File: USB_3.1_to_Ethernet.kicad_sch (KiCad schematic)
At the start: 5 parts, among them J1 RJ45_JK0654219, U1 LAN7801_9JX, U2 93LC56B_SN, U3 KSZ9031RNXCC, U4 TLV76733QWDRBxQ1

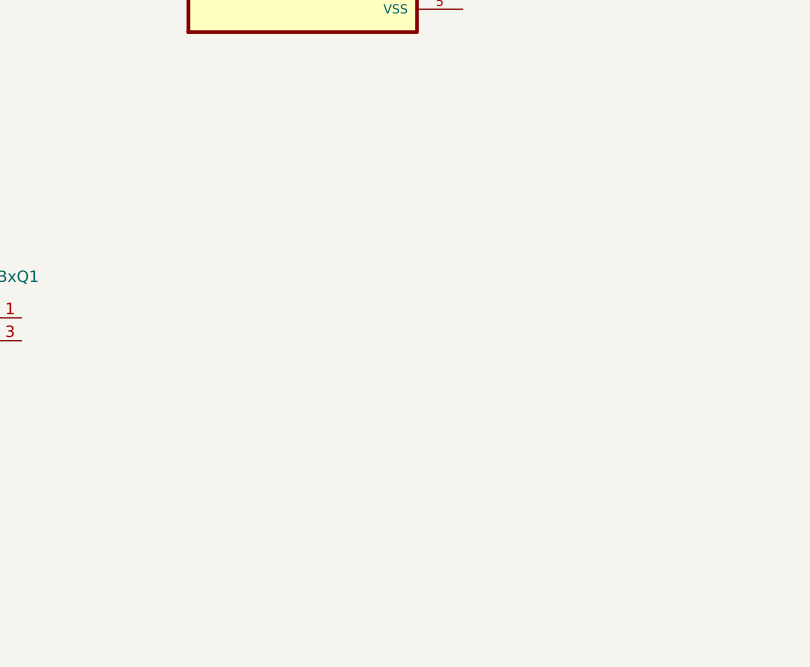
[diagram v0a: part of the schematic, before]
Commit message: usb connector added
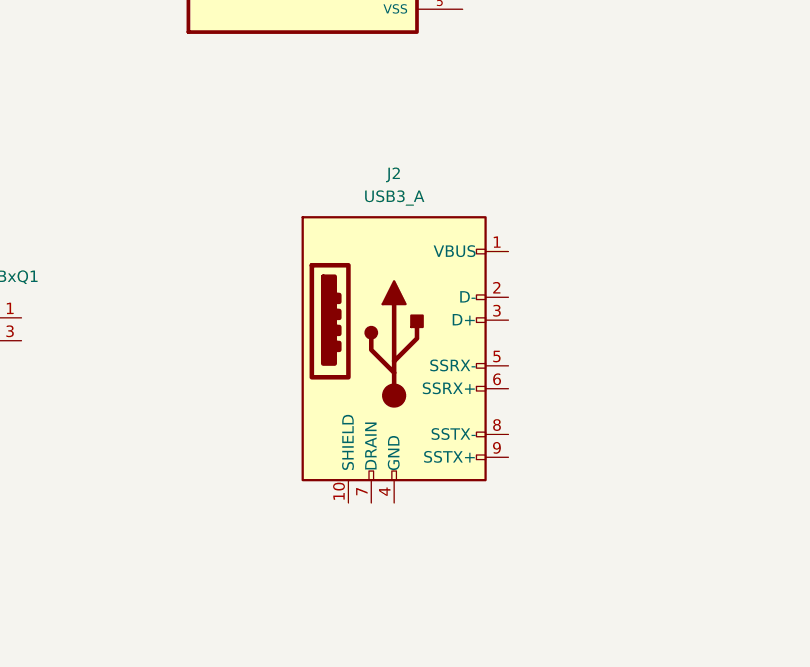
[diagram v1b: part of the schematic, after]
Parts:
- added J2: USB3_A, Connector_USB:USB3_A_Plug_Wuerth_692112030100_Horizontal, symbol Connector:USB3_A
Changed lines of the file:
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@@
+	)
+	(symbol
+		(lib_id "Connector:USB3_A")
+		(at 159.258 119.126 0)
+		(unit 1)
+		(exclude_from_sim no)
+		(in_bom yes)
+		(on_board yes)
+		(dnp no)
+		(fields_autoplaced yes)
+		(property "Reference" "J2"
+			(at 159.258 100.33 0)
+			(effects
+				(font
+					(size 1.27 1.27)
+				)
+			)
+		)
+		(property "Value" "USB3_A"
+			(at 159.258 102.87 0)
+			(effects
+				(font
+					(size 1.27 1.27)
+				)
+			)
+		)
+		(property "Footprint" "Connector_USB:USB3_A_Plug_Wuerth_692112030100_Horizontal"
+			(at 163.068 116.586 0)
+			(effects
+				(font
+					(size 1.27 1.27)
+				)
+				(hide yes)
+			)
+		)
+		(property "Datasheet" "~"
+			(at 163.068 116.586 0)
+			(effects
+				(font
+					(size 1.27 1.27)
+				)
+				(hide yes)
+			)
+		)
+		(property "Description" "USB 3.0 A connector"
+			(at 159.258 119.126 0)
+			(effects
+				(font
+					(size 1.27 1.27)
+				)
+				(hide yes)
+			)
+		)
+		(pin "4"
+		)
+		(pin "7"
+		)
+		(pin "3"
+		)
+		(pin "5"
+		)
+		(pin "1"
+		)
+		(pin "2"
+		)
+		(pin "8"
+		)
+		(pin "9"
+		)
+		(pin "6"
+		)
+		(pin "10"
+		)
+		(instances
+			(project ""
+				(path "/b00c1253-ab18-4b3e-8546-134ebc6e3f42"
+					(reference "J2")
+					(unit 1)
+				)
+			)
+		)
 	)
 	(symbol

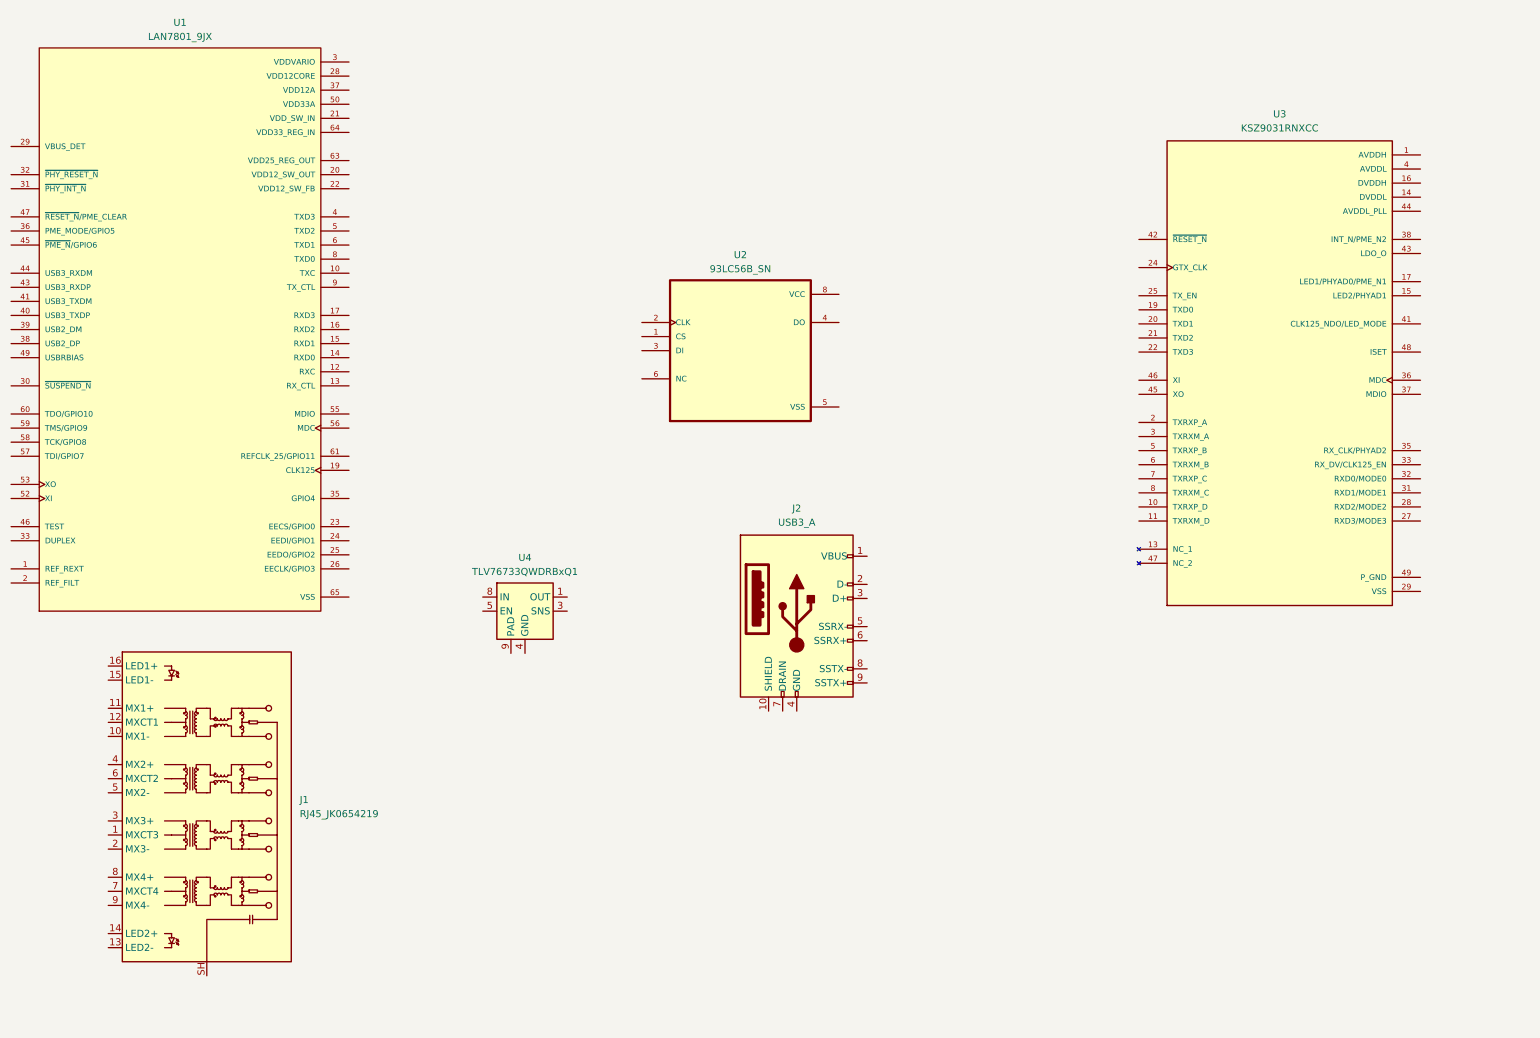
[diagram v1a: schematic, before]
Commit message: tvs-FB-ldo-symbol-footprint
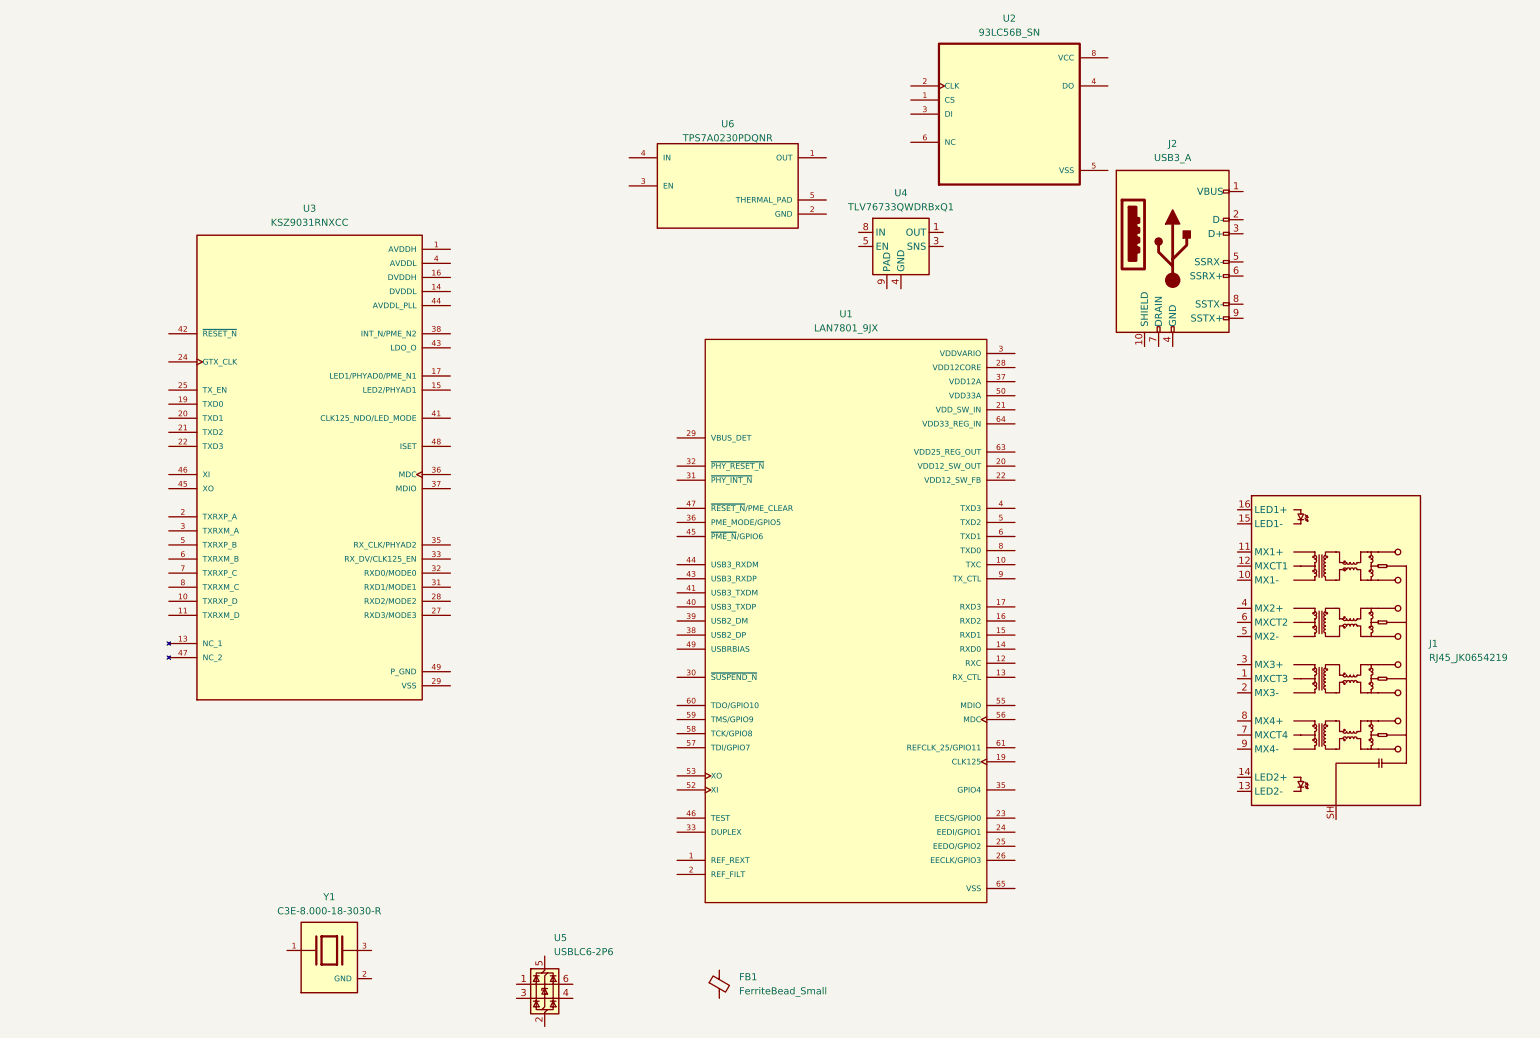
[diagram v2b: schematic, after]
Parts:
- added FB1: FerriteBead_Small, Inductor_SMD:L_0603_1608Metric_Pad1.05x0.95mm_HandSolder, symbol Device:FerriteBead_Small
- added U5: USBLC6-2P6, Package_TO_SOT_SMD:SOT-666, symbol Power_Protection:USBLC6-2P6
- added U6: TPS7A0230PDQNR, TPS7A0230PDQNR:IC_TPS7A0230PDQNR, symbol TPS7A0230PDQNR:TPS7A0230PDQNR
- added Y1: C3E-8.000-18-3030-R, C3E-8.000-18-3030-R:XTAL_C3E-8.000-18-3030-R, symbol C3E-8.000-18-3030-R:C3E-8.000-18-3030-R
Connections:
- new net GND: Y1.2 (GND), Y1.4 (GND)
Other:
- moved on the sheet: J1, J2, U1, U2, U3, U4

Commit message: power section added and power connections done
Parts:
- removed FB1: FerriteBead_Small, Inductor_SMD:L_0603_1608Metric_Pad1.05x0.95mm_HandSolder, symbol Device:FerriteBead_Small
- removed J2: USB3_A, Connector_USB:USB3_A_Plug_Wuerth_692112030100_Horizontal, symbol Connector:USB3_A
- removed U4: TLV76733QWDRBxQ1, Package_SON:VSON-8-1EP_3x3mm_P0.65mm_EP1.65x2.4mm_ThermalVias, symbol Regulator_Linear:TLV76733QWDRBxQ1
- removed U5: USBLC6-2P6, Package_TO_SOT_SMD:SOT-666, symbol Power_Protection:USBLC6-2P6
- removed U6: TPS7A0230PDQNR, TPS7A0230PDQNR:IC_TPS7A0230PDQNR, symbol TPS7A0230PDQNR:TPS7A0230PDQNR
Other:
- added sheet Power section (untitled.kicad_sch)
- moved on the sheet: J1, U1, U2, U3
